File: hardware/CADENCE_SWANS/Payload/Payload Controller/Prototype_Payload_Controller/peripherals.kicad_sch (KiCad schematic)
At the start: 0 parts

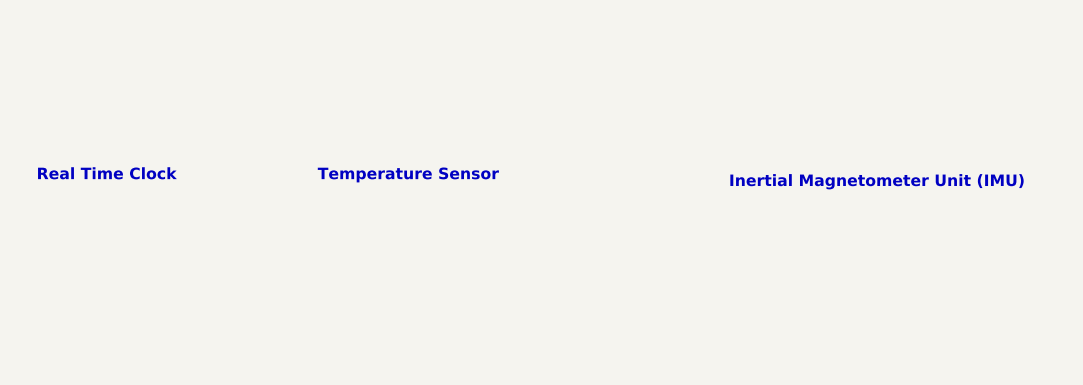
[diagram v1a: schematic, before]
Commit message: added SN65C1668 symbol library and a folder for symbols
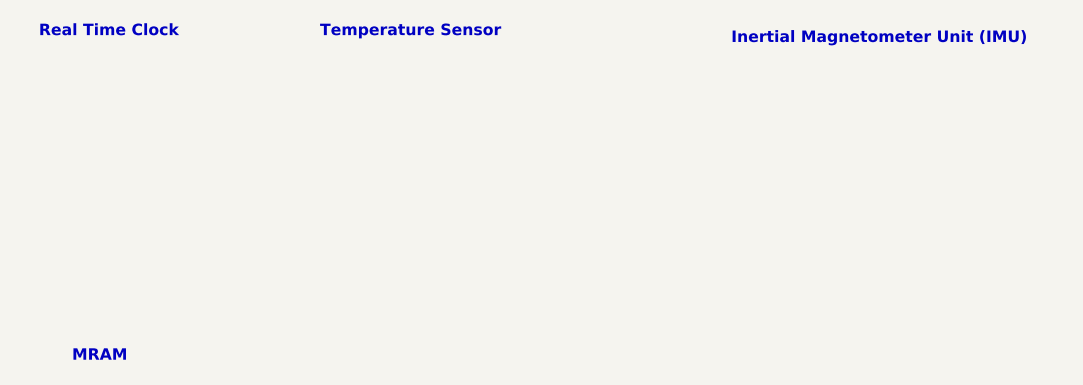
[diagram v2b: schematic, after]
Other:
- note added: "MRAM"
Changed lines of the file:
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@@
 	(text "Inertial Magnetometer Unit (IMU)"
 		(exclude_from_sim no)
-		(at 148.336 65.532 0)
+		(at 148.59 49.53 0)
+		(effects
+			(font
+				(size 1.27 1.27)
+				(thickness 0.254)
+				(bold yes)
+			)
+		)
+	)
+	(text "MRAM"
+		(exclude_from_sim no)
+		(at 61.976 84.836 0)
 		(effects
 			(font
@@
 	(text "Real Time Clock"
 		(exclude_from_sim no)
-		(at 62.738 64.77 0)
+		(at 62.992 48.768 0)
 		(effects
 			(font
@@
 	(text "Temperature Sensor"
 		(exclude_from_sim no)
-		(at 96.266 64.77 0)
+		(at 96.52 48.768 0)
 		(effects
 			(font
